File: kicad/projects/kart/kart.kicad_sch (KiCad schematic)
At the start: 44 parts, among them J2 Servo, J3 Motor_Driver, J4 2S Lipo, J5 Speaker, J6 WS2812b, J7 IR LEDs, J8 Beleuchtung, J9 Rückwärts, Q1 MMBT2222A, Q2 Beleuchtung, Q3 Beleuchtung, SW1 Characterwähler, SW2 SW_DP3T, U1 ESP32-C6-SUPERMINI, U2 DFPlayer Mini, U3 LSM6DS3, U6 AP63205WU

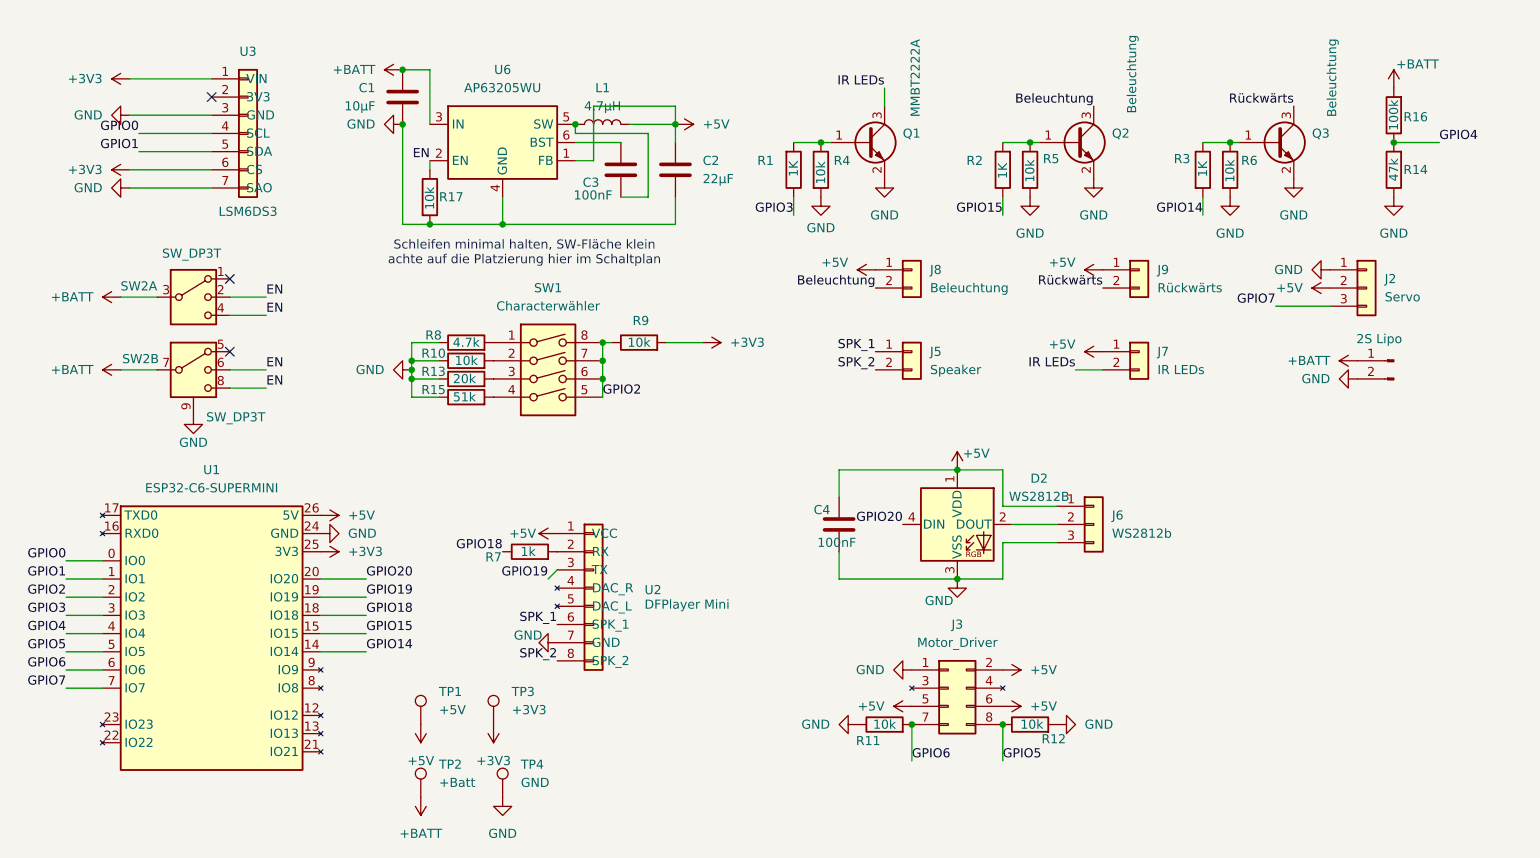
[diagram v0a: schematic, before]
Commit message: Repo für Veröffentlichung vorbereitet: KiCad-Struktur, Lizenz, Aufräumen
- KiCad-Projekte je Platine nach kicad/projects/<board>/ (kart, controller,
  buttons, switch), eigene Bibliotheken nach kicad/libs/, projektlokale
  sym-lib-table/fp-lib-table auf ${KIPRJMOD}/../../libs
- Schalter-Platinchen: einschalter -> switch, Titelblock vereinheitlicht
- AO4407A: 3D-Modell auf KiCad-Standard-SOIC-8, Footprint-Verweis korrigiert
- Alte Stände nach kicad/archive/ (FB-V1-Layout, D1-Mini-Schaltplan)
- Lizenz CC BY-NC-SA 4.0, Fan-Projekt-Hinweis
- CLAUDE.md nicht mehr versioniert, PDFs/DOCX/Exporte ignoriert
- Laufende Firmware-Änderungen (Kart V2, FB V2, Stern-Licht) mitcommittet
- docs/wiki-plan.md: Arbeitsliste für das Wiki

Co-Authored-By: Claude Opus 5.5 <noreply@anthropic.com>
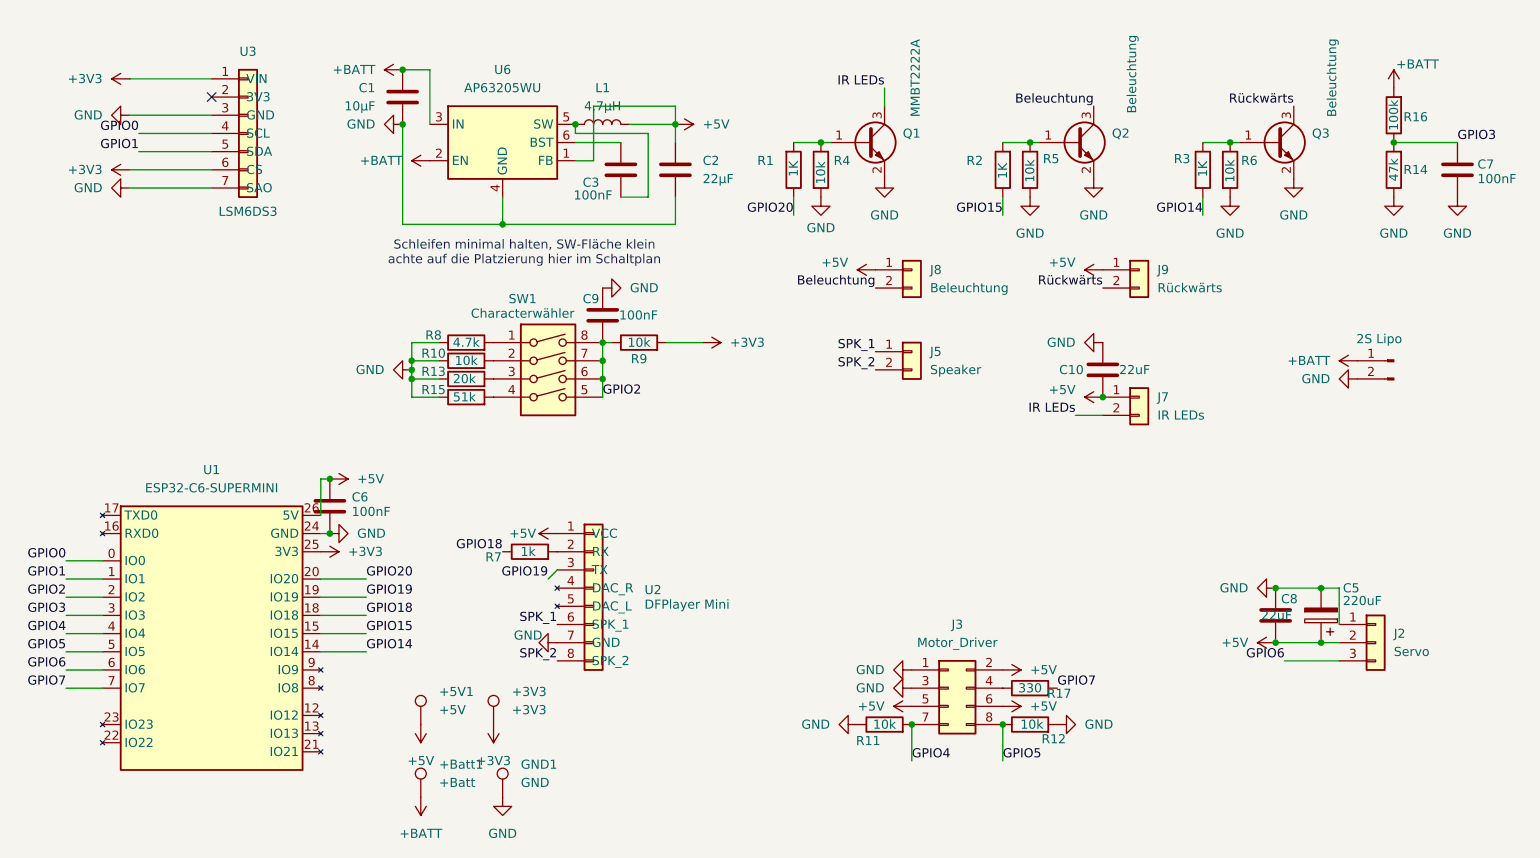
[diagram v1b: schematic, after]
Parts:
- removed C4: 100nF, Capacitor_SMD:C_0805_2012Metric_Pad1.18x1.45mm_HandSolder, symbol Device:C
- removed D2: WS2812B, LED_SMD:LED_WS2812B_PLCC4_5.0x5.0mm_P3.2mm, symbol LED:WS2812B
- removed J6: WS2812b, Connector_JST:JST_XH_B3B-XH-A_1x03_P2.50mm_Vertical, symbol Connector_Generic:Conn_01x03
- removed SW2: SW_DP3T, zzzz_Own:SW_Slide_2P3T_8pin_P2.0mm_MountingLugs, symbol Switch:SW_DP3T
- added C10, C8: 22uF, Capacitor_SMD:C_1206_3216Metric_Pad1.33x1.80mm_HandSolder, symbol Device:C
- added C5: 220uF, Capacitor_SMD:CP_Elec_6.3x5.4, symbol Device:C_Polarized
- added C6, C7, C9: 100nF, Capacitor_SMD:C_0805_2012Metric_Pad1.18x1.45mm_HandSolder, symbol Device:C
- J4: footprint Connector_Wire:SolderWire-1.5sqmm_1x02_P6mm_D1.7mm_OD3mm -> Connector_Wire:SolderWire-0.75sqmm_1x02_P4.8mm_D1.25mm_OD2.3mm
- J5, J7, J8, J9: footprint Connector_JST:JST_XH_B2B-XH-A_1x02_P2.50mm_Vertical -> Connector_PinHeader_2.54mm:PinHeader_1x02_P2.54mm_Vertical
- R17: value 10k -> 330
- renumbered TP3 to +3V3, TP1 to +5V1, TP2 to +Batt1, TP4 to GND1
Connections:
- net +5V: now also C10.2, C5.1, C6.1, C8.2
- net +BATT: now also U6.2 (EN)
- net GND: now also J3.3 (Pin_3), C10.1, C5.2, C6.2, C7.2, C8.1, C9.1; no longer R17.2
- net GPIO2: now also C9.2
- net GPIO20: now also R1.1
- net GPIO3: now also R14.2, R16.1, C7.1; no longer R1.1
- net GPIO4: now also J3.7 (Pin_7), R11.2; no longer R14.2, R16.1
- net GPIO6: now also J2.3 (Pin_3); no longer J3.7 (Pin_7), R11.2
- net GPIO7: now also R17.2; no longer J2.3 (Pin_3)
- net at J3.4 (Pin_4): now also R17.1
- removed net EN: R17.1, U6.2 (EN)
- no-connect marks 3 -> 1
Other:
- title: Mario Kart Platine -> Mario Kart PCB
- moved on the sheet: J2, J7
